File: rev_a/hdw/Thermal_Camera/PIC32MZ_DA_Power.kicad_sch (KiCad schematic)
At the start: 18 parts

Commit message: finished PIC32MZ DA symbol
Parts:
- added U?: PIC32MZ2064DAR176, Custom Footprints Library:LQFP-176_20x20mm_P0.4mm_7p9x7p9mm_EP, symbol Custom Library:PIC32MZ2064DAR176
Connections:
- net GND: now also U?.103 (VSS), U?.115 (VSS), U?.122 (VSS), U?.123 (VSS), U?.153 (VSS), U?.154 (VSS), U?.177 (VSS1P8), U?.21 (VSS), U?.22 (VSS), U?.29 (VSS), U?.37 (VSS), U?.48 (VSS), U?.49 (VSS), U?.83 (VSS), U?.87 (VSS), U?.94 (VSS)
- new net ~{PIC32MZ_MCLR}: U?.85 (MCLR)
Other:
- moved on the sheet: C?, L?

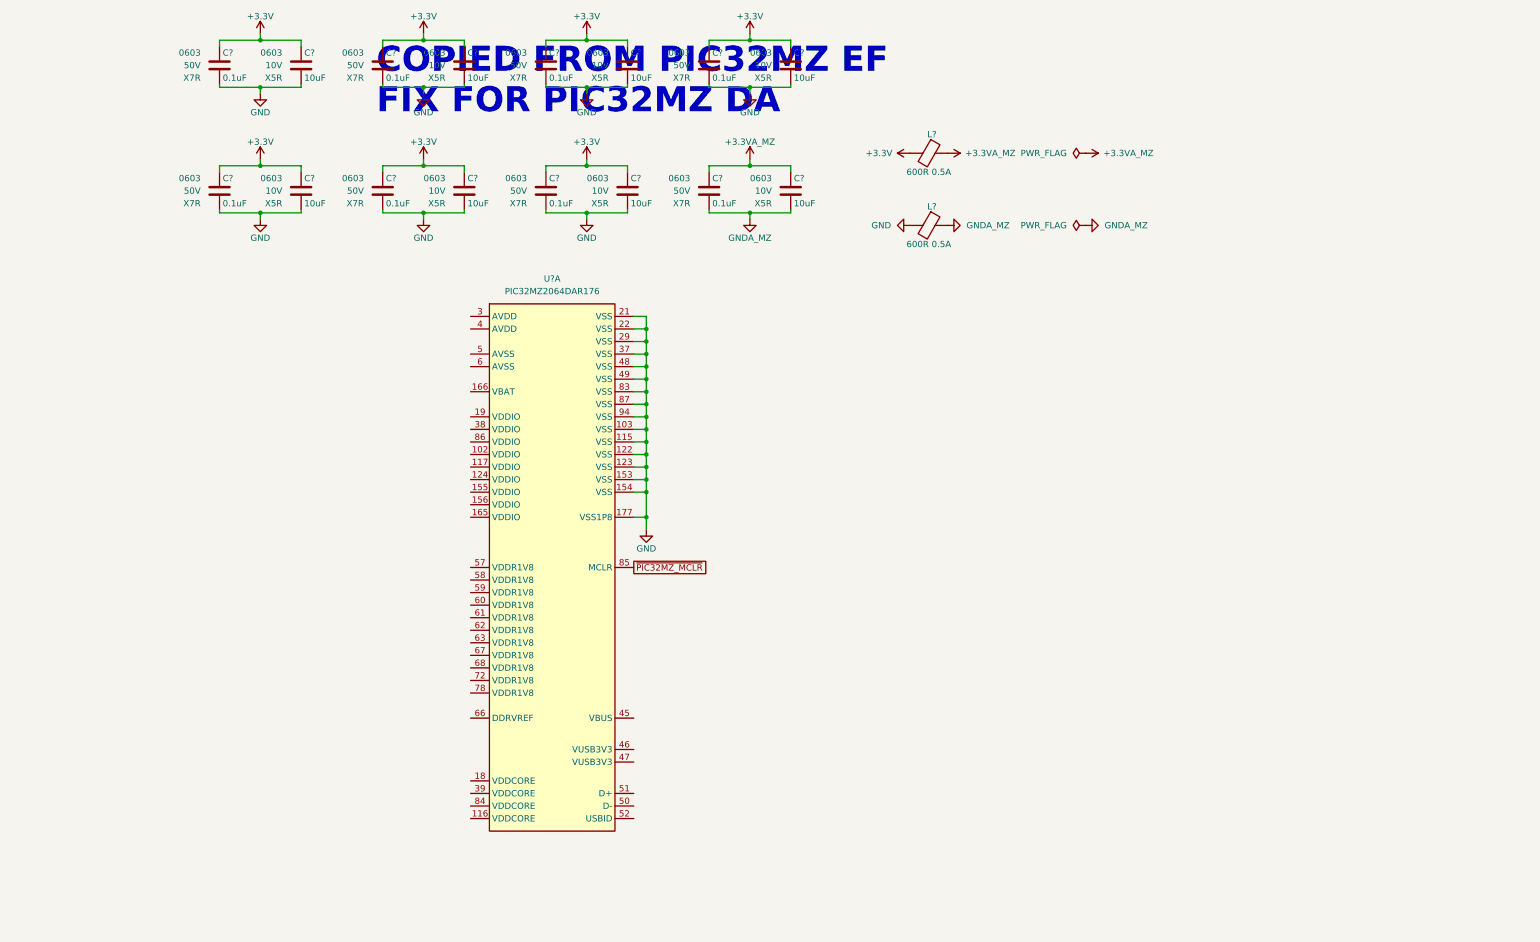
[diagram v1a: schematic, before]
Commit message: added lepton sensor, made some other schematic progress
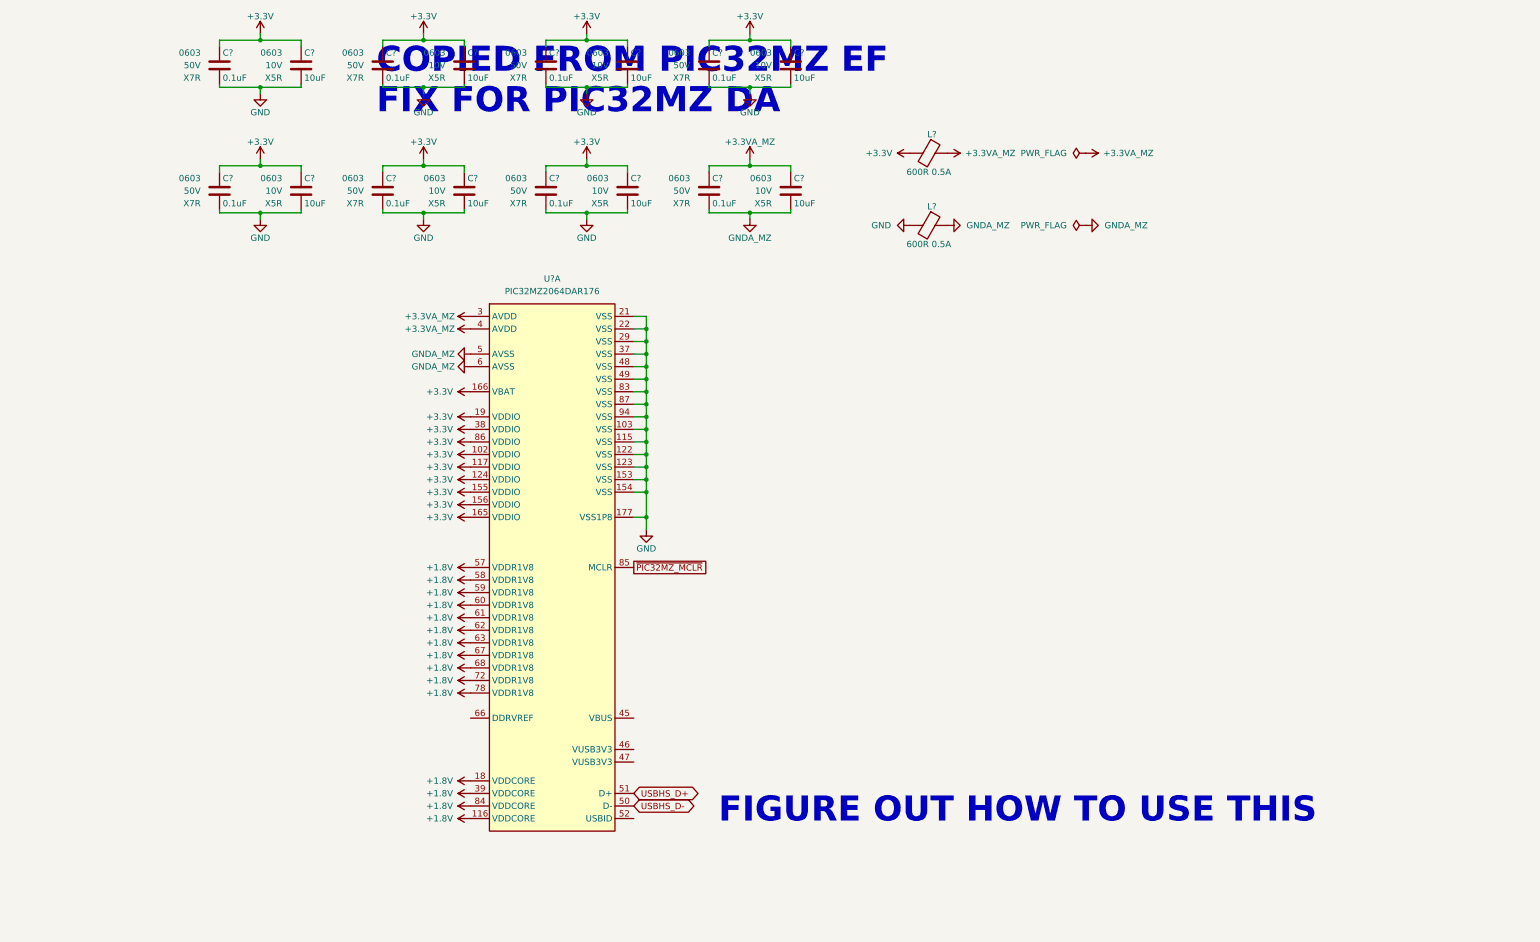
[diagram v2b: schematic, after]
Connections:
- net +3.3V: now also U?.102 (VDDIO), U?.117 (VDDIO), U?.124 (VDDIO), U?.155 (VDDIO), U?.156 (VDDIO), U?.165 (VDDIO), U?.166 (VBAT), U?.19 (VDDIO), U?.38 (VDDIO), U?.86 (VDDIO)
- net +3.3VA_MZ: now also U?.3 (AVDD), U?.4 (AVDD)
- net GNDA_MZ: now also U?.5 (AVSS), U?.6 (AVSS)
- net +1.8V: now reaches U?.116 (VDDCORE)
- net +1.8V: now also U?.18 (VDDCORE), U?.39 (VDDCORE), U?.57 (VDDR1V8), U?.58 (VDDR1V8), U?.59 (VDDR1V8), U?.60 (VDDR1V8), U?.61 (VDDR1V8), U?.62 (VDDR1V8), U?.63 (VDDR1V8), U?.67 (VDDR1V8), U?.68 (VDDR1V8), U?.72 (VDDR1V8), U?.78 (VDDR1V8), U?.84 (VDDCORE)
- net USBHS_D-: now reaches U?.50 (D-)
- net USBHS_D+: now reaches U?.51 (D+)
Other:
- note added: "FIGURE OUT HOW TO USE THIS"

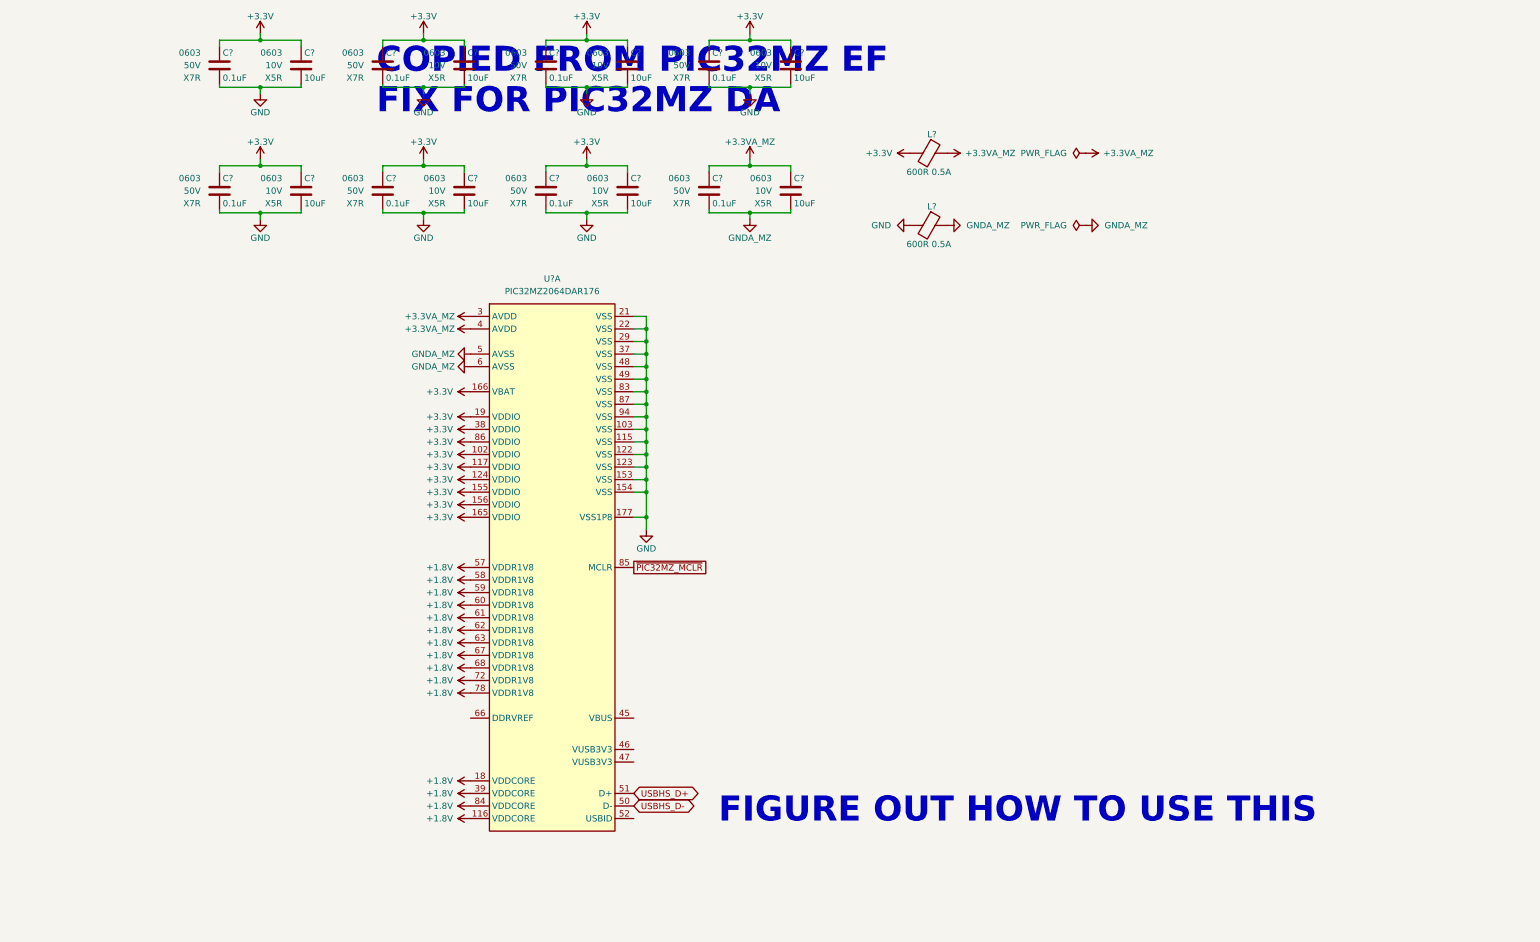
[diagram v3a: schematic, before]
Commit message: changed a lot of circuits from +3.3V to +3.0V VDD
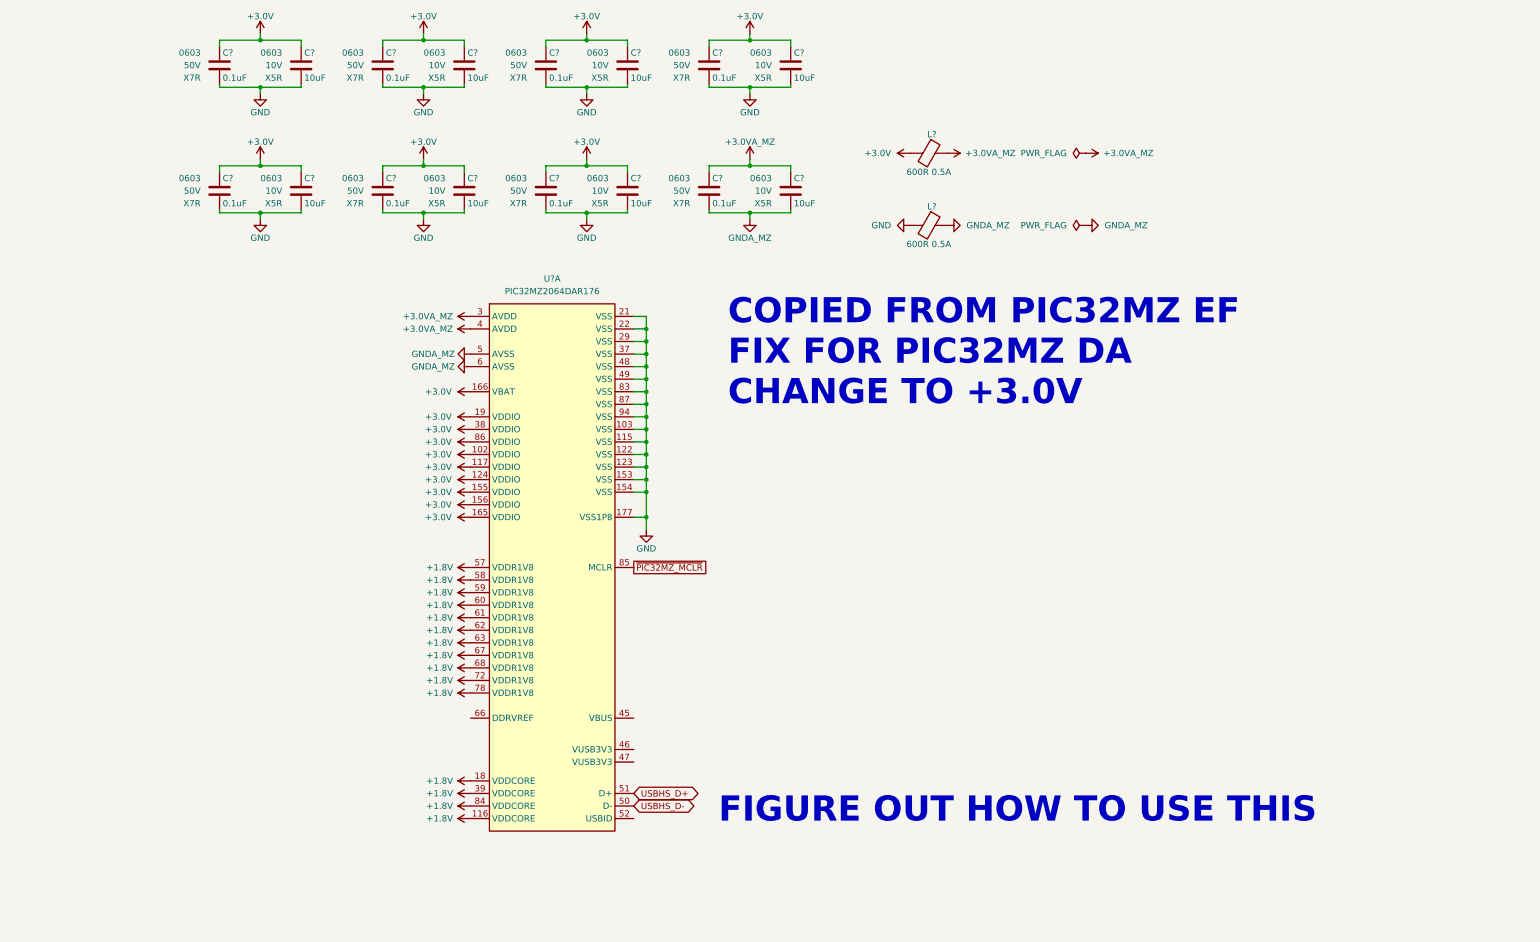
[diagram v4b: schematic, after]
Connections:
- net +3.3V renamed +3.0V
- net +3.3VA_MZ renamed +3.0VA_MZ
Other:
- note added: "COPIED FROM PIC32MZ EF FIX FOR PIC32MZ DA CHANGE TO +3.0V"
- note removed: "COPIED FROM PIC32MZ EF FIX FOR PIC32MZ DA"

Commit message: added PIC32 bypass, SD card load switch, other random junk
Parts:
- removed C? (x7): 10uF, Capacitors_SMD:C_0603, symbol Custom_Library:C_Custom
- added C? (x23): 0.1uF, Capacitors_SMD:C_0603, symbol Custom_Library:C_Custom
- added C? (x30): 0.01uF, Capacitors_SMD:C_0603, symbol Custom_Library:C_Custom
- C?: value 10uF -> 0.01uF; Digi-Key PN 1276-1871-1-ND -> (none); Voltage 10V -> 50V
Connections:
- net +1.8V: now also C?.1, C?.1, C?.1, C?.1, C?.1, C?.1, C?.1, C?.1, C?.1, C?.1, C?.1, C?.1, C?.1, C?.1, C?.1, C?.1, C?.1, C?.1, C?.1, C?.1, C?.1, C?.1, C?.1, C?.1, C?.1, C?.1, C?.1, C?.1, C?.1, C?.1
- net +3.0V: now also C?.1, C?.1, C?.1, C?.1, C?.1, C?.1, C?.1, C?.1, C?.1, C?.1, C?.1, C?.1
- net +3.0VA_MZ: now also C?.1, C?.1, C?.1
- net GND: now also C?.2, C?.2, C?.2, C?.2, C?.2, C?.2, C?.2, C?.2, C?.2, C?.2, C?.2, C?.2, C?.2, C?.2, C?.2, C?.2, C?.2, C?.2, C?.2, C?.2, C?.2, C?.2, C?.2, C?.2, C?.2, C?.2, C?.2, C?.2, C?.2, C?.2, C?.2, C?.2, C?.2, C?.2, C?.2, C?.2, C?.2, C?.2, C?.2, C?.2, C?.2, C?.2, C?.2, C?.2, C?.2, C?.2, C?.2, C?.2, C?.2, C?.2
- net GNDA_MZ: now also C?.2, C?.2, C?.2
- net +5V_USB: now reaches U?.45 (VBUS)
- net +5V_USB: now also C?.1, C?.1
- net +3.3V_USB_MZ: now reaches U?.46 (VUSB3V3)
- net +3.3V_USB_MZ: now also U?.47 (VUSB3V3), C?.1, C?.1, C?.1, C?.1
- net VMEM_REF: now reaches U?.66 (DDRVREF)
- net VMEM_REF: now also C?.1, C?.1
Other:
- note removed: "COPIED FROM PIC32MZ EF FIX FOR PIC32MZ DA CHANGE TO +3.0V"
- moved on the sheet: C?, L?, U?A

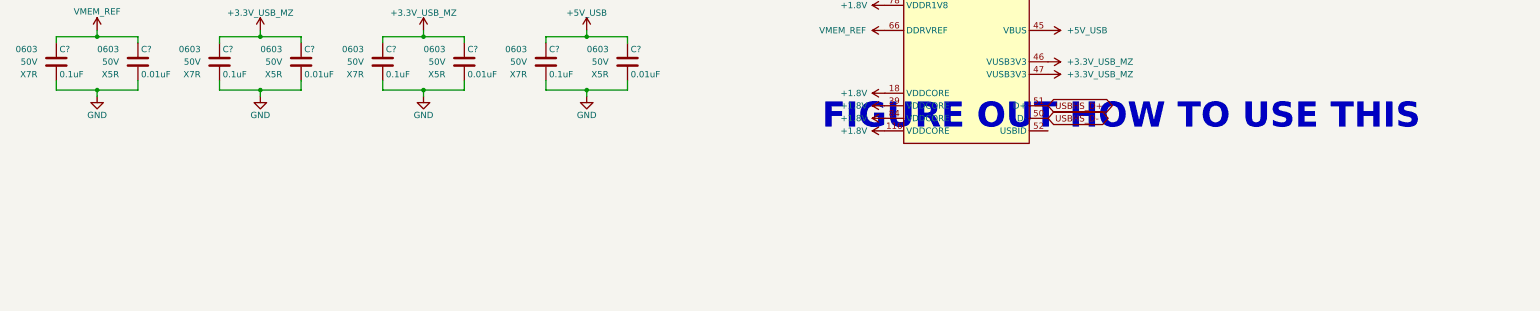
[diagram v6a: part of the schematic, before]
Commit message: added some USB stuff
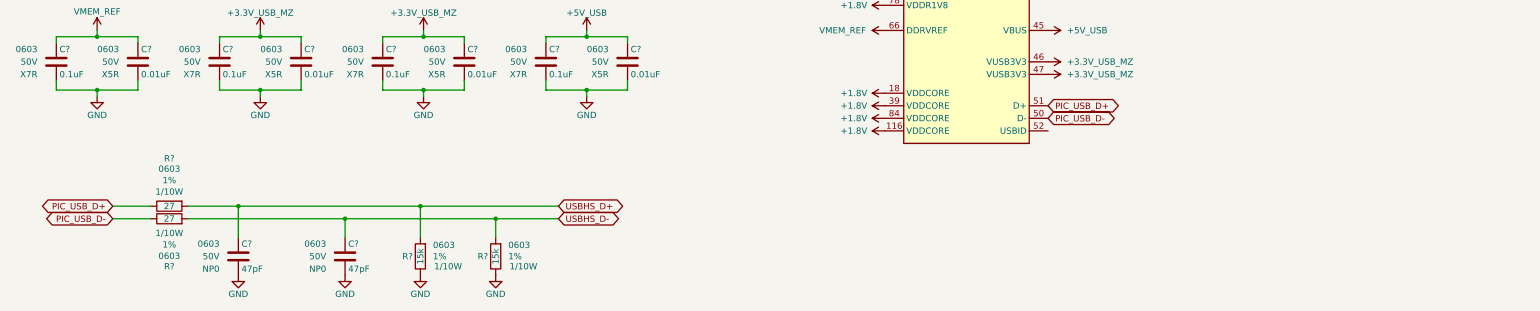
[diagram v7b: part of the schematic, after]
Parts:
- added C? (x2): 47pF, Capacitors_SMD:C_0603, symbol Custom_Library:C_Custom
- added R? (x2): 15k, Resistors_SMD:R_0603, symbol Custom_Library:R_Custom
- added R? (x2): 27, Resistors_SMD:R_0603, symbol Custom_Library:R_Custom
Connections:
- net GND: now also C?.2, C?.2, R?.2, R?.2
- net USBHS_D+: now also C?.1, R?.1, R?.1; no longer U?.51 (D+)
- net USBHS_D-: now also C?.1, R?.1, R?.1; no longer U?.50 (D-)
- new net PIC_USB_D+: R?.2, U?.51 (D+)
- new net PIC_USB_D-: R?.2, U?.50 (D-)
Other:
- note removed: "FIGURE OUT HOW TO USE THIS"
